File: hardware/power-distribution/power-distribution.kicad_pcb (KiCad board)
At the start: 2 copper layers, 100 x 100 mm, 54 parts, among them J1 Conn_01x02_Male, J10 Screw_Terminal_01x02, J11 Screw_Terminal_01x02, J12 Screw_Terminal_01x02, J13 Screw_Terminal_01x02, J14 Conn_01x02, J15 Screw_Terminal_01x06, J2 Conn_01x02_Male, J3 Conn_01x02_Male, J4 Conn_01x02_Male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

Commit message: Routed PCB
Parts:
- removed C1, C2, C3, C4, C5, C6: C, Capacitor_SMD:C_0603_1608Metric_Pad1.05x0.95mm_HandSolder
- removed F5, F6: Fuse, Highside-powerdistribution:ATO_Fuseholder_3522-2
- removed J10, J11, J12, J13, J8, J9: Screw_Terminal_01x02, Highside-powerdistribution:PTSA1,5-2-3,5-Z
- removed J14: Conn_01x02, Highside-powerdistribution:Phoenix_TB_2-1935776
- removed J15: Screw_Terminal_01x06, Highside-powerdistribution:20.101M-6
- removed J4, J5: Conn_01x02_Male, Connector_PinHeader_2.54mm:PinHeader_1x02_P2.54mm_Vertical
- removed Q5, Q6: P-MOSFET, Highside-powerdistribution:PG-TO263-3-2
- removed R10, R11, R12, R5, R6, R7, R8, R9: R, Resistor_SMD:R_0603_1608Metric_Pad1.05x0.95mm_HandSolder
- removed the REF** at (57.0, 91.0)
- removed the REF** at (146.5, 81.0)
- removed the REF** at (140.5, 76.0)
- removed the REF** at (52.5, 86.0)
- removed the REF** at (146.5, 53.5)
- removed the REF** at (53.5, 53.5)
- removed the REF** at (146.5, 146.5)
- removed the REF** at (146.5, 101.0)
- removed the REF** at (146.5, 91.0)
- removed the REF** at (140.5, 96.0)
- removed the REF** at (140.5, 86.0)
- added POWER_IN1: Screw_Terminal_01x02, TerminalBlock_Phoenix:TerminalBlock_Phoenix_PT-1,5-2-5.0-H_1x02_P5.00mm_Horizontal, F.Cu at (65.0, 105.0)
- added POWER_OUT1: Screw_Terminal_01x04, TerminalBlock_Phoenix:TerminalBlock_Phoenix_PT-1,5-4-5.0-H_1x04_P5.00mm_Horizontal, F.Cu at (120.0, 115.0)
- added REF**: MountingHole_3.2mm_M3_Pad_Via, MountingHole:MountingHole_3.2mm_M3_Pad_Via, F.Cu at (135.0, 85.0)
- added REF**: MountingHole_3.2mm_M3_Pad_Via, MountingHole:MountingHole_3.2mm_M3_Pad_Via, F.Cu at (135.0, 145.0)
- added REF**: MountingHole_3.2mm_M3_Pad_Via, MountingHole:MountingHole_3.2mm_M3_Pad_Via, F.Cu at (55.0, 145.0)
- added REF**: MountingHole_3.2mm_M3_Pad_Via, MountingHole:MountingHole_3.2mm_M3_Pad_Via, F.Cu at (55.0, 85.0)
- added SWITCH_A1: Screw_Terminal_01x0, TerminalBlock_Phoenix:TerminalBlock_Phoenix_PT-1,5-2-5.0-H_1x02_P5.00mm_Horizontal, F.Cu at (100.0, 137.5)
- added SWITCH_B1: Screw_Terminal_01x02, TerminalBlock_Phoenix:TerminalBlock_Phoenix_PT-1,5-2-5.0-H_1x02_P5.00mm_Horizontal, F.Cu at (87.5, 137.5)
- added SWITCH_C1: Screw_Terminal_01x02, TerminalBlock_Phoenix:TerminalBlock_Phoenix_PT-1,5-2-5.0-H_1x02_P5.00mm_Horizontal, F.Cu at (75.0, 137.5)
- added SWITCH_C2: Screw_Terminal_01x02, TerminalBlock_Phoenix:TerminalBlock_Phoenix_PT-1,5-2-5.0-H_1x02_P5.00mm_Horizontal, F.Cu at (62.5, 137.5)
- F1, F2, F3, F4: footprint Highside-powerdistribution:ATO_Fuseholder_3522-2 -> Private Fuses:ATO_Fuseholder_3522-2
- J1, J2, J3: value Conn_01x02_Male -> Parallell
- Q1, Q2, Q3, Q4: value P-MOSFET -> Q_PMOS_GDS; footprint Highside-powerdistribution:PG-TO263-3-2 -> Package_TO_SOT_SMD:TO-252-2
- R1, R2, R3, R4: value R -> 10k
- moved R4 25.6 mm to (67.5, 130.0), turned to 270 degrees
- moved R2 15.1 mm to (87.5, 130.0), turned to 270 degrees
- moved F4 14.5 mm to (102.5, 92.5)
- moved R3 13.4 mm to (80.0, 130.0), turned to 270 degrees
- moved F3 12.8 mm to (102.5, 102.5)
- moved Q4 11.4 mm to (85.0, 92.5), turned to 0 degrees
- moved F2 11.4 mm to (102.5, 112.5)
- moved F1 10.4 mm to (102.5, 122.5)
- moved Q3 8.99 mm to (85.4, 102.5), turned to 0 degrees
- moved Q2 7.11 mm to (85.0, 112.5), turned to 0 degrees
- moved J3 6.96 mm to (72.5, 130.0), turned to 270 degrees
- moved Q1 5.08 mm to (85.4, 122.5), turned to 0 degrees
- moved J2 4.30 mm to (85.0, 130.0), turned to 270 degrees
- moved R1 3.62 mm to (100.0, 130.0), turned to 270 degrees
- moved J1 2.55 mm to (97.5, 130.0), turned to 270 degrees
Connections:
- J1 pad 1: Net-(C1-Pad1) -> /G1
- J1 pad 2: Net-(C2-Pad1) -> Net-(J1-Pad2)
- J2 pad 1: Net-(C2-Pad1) -> Net-(J1-Pad2)
- J2 pad 2: Net-(C3-Pad1) -> Net-(J2-Pad2)
- J3 pad 1: Net-(C3-Pad1) -> Net-(J2-Pad2)
- J3 pad 2: Net-(C4-Pad1) -> Net-(J3-Pad2)
- Q1 pad 1: Net-(C1-Pad1) -> /G1
- Q1 pad 2: +12V -> SSR-A
- Q1 pad 3: SSR-A -> +12V
- Q2 pad 1: Net-(C2-Pad1) -> Net-(J1-Pad2)
- Q2 pad 2: +12V -> SSR-B
- Q2 pad 3: SSR-B -> +12V
- Q3 pad 1: Net-(C3-Pad1) -> Net-(J2-Pad2)
- Q3 pad 2: +12V -> SSR-C
- Q3 pad 3: SSR-C -> +12V
- Q4 pad 1: Net-(C4-Pad1) -> Net-(J3-Pad2)
- Q4 pad 2: +12V -> SSR-D
- Q4 pad 3: SSR-D -> +12V
- R1 pad 1: Net-(C1-Pad1) -> +12V
- R1 pad 2: +12V -> /G1
- R2 pad 1: Net-(J8-Pad1) -> +12V
- R2 pad 2: Net-(C1-Pad1) -> Net-(J1-Pad2)
- R3 pad 1: Net-(C2-Pad1) -> +12V
- R3 pad 2: +12V -> Net-(J2-Pad2)
- R4 pad 1: Net-(J9-Pad1) -> +12V
- R4 pad 2: Net-(C2-Pad1) -> Net-(J3-Pad2)
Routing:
- net Net-(C6-Pad1): track 103.5 -> 0.00 mm, vias 2 -> 0
- net GND: track 212.2 -> 111.8 mm, vias 6 -> 0
- net Net-(C5-Pad1): track 87.1 -> 0.00 mm, vias 2 -> 0
- net Net-(C4-Pad1): track 66.9 -> 0.00 mm, vias 2 -> 0
- net Net-(J3-Pad2): track 0.00 -> 60.4 mm, vias 0 -> 1
- net Net-(C3-Pad1): track 58.4 -> 0.00 mm, vias 2 -> 0
- net Net-(F1-Pad1): track 57.6 -> 0.00 mm
- net Net-(F6-Pad1): track 55.6 -> 0.00 mm
- net Net-(C2-Pad1): track 53.2 -> 0.00 mm, vias 2 -> 0
- net Net-(J2-Pad2): track 0.00 -> 49.3 mm, vias 0 -> 1
- net Net-(F5-Pad1): track 44.9 -> 0.00 mm
- net Net-(F2-Pad1): track 44.8 -> 0.00 mm
- net Net-(C1-Pad1): track 43.1 -> 0.00 mm, vias 2 -> 0
- net Net-(J1-Pad2): track 0.00 -> 39.5 mm, vias 0 -> 1
- net Net-(F3-Pad1): track 36.3 -> 0.00 mm
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- added copper zone on B.Cu, net Net-(F1-Pad1)
- added copper zone on F.Cu, net Net-(F1-Pad1)
- added copper zone on B.Cu, net Net-(F2-Pad1)
- added copper zone on F.Cu, net Net-(F2-Pad1)
- removed copper zone on B.Cu, net SSR-E
- removed copper zone on F.Cu, net SSR-E
- removed copper zone on B.Cu, net SSR-F
- removed copper zone on F.Cu, net SSR-F
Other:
- board size 100 x 100 mm -> 90 x 70 mm
- board text added: "MAX 18 A continuous (200 W)"
- board text added: "Rev 2 2020-03-12"
- board text removed: "E"
- board text removed: "F"
- board text removed: "Rev 1.3 2020-01-08"

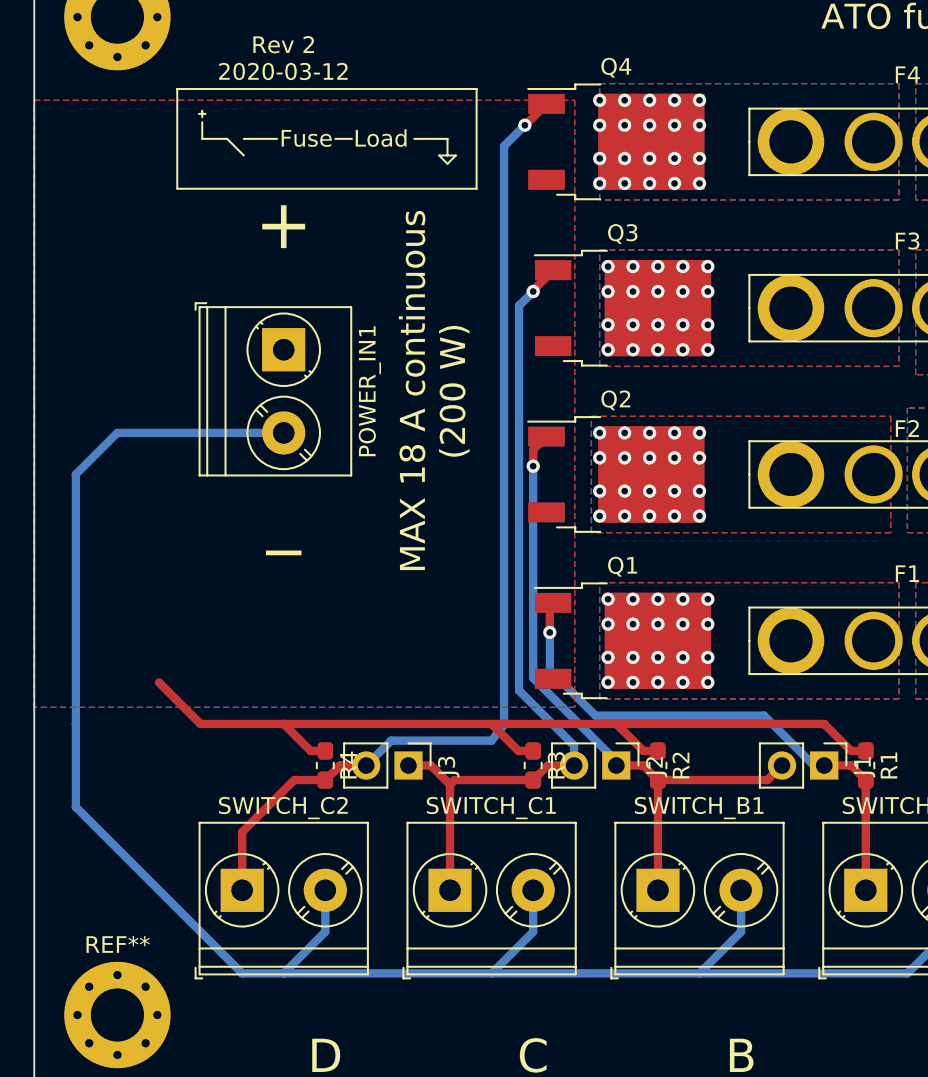
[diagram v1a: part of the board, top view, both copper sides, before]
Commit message: Runned ERC/DRC and exported gerber files
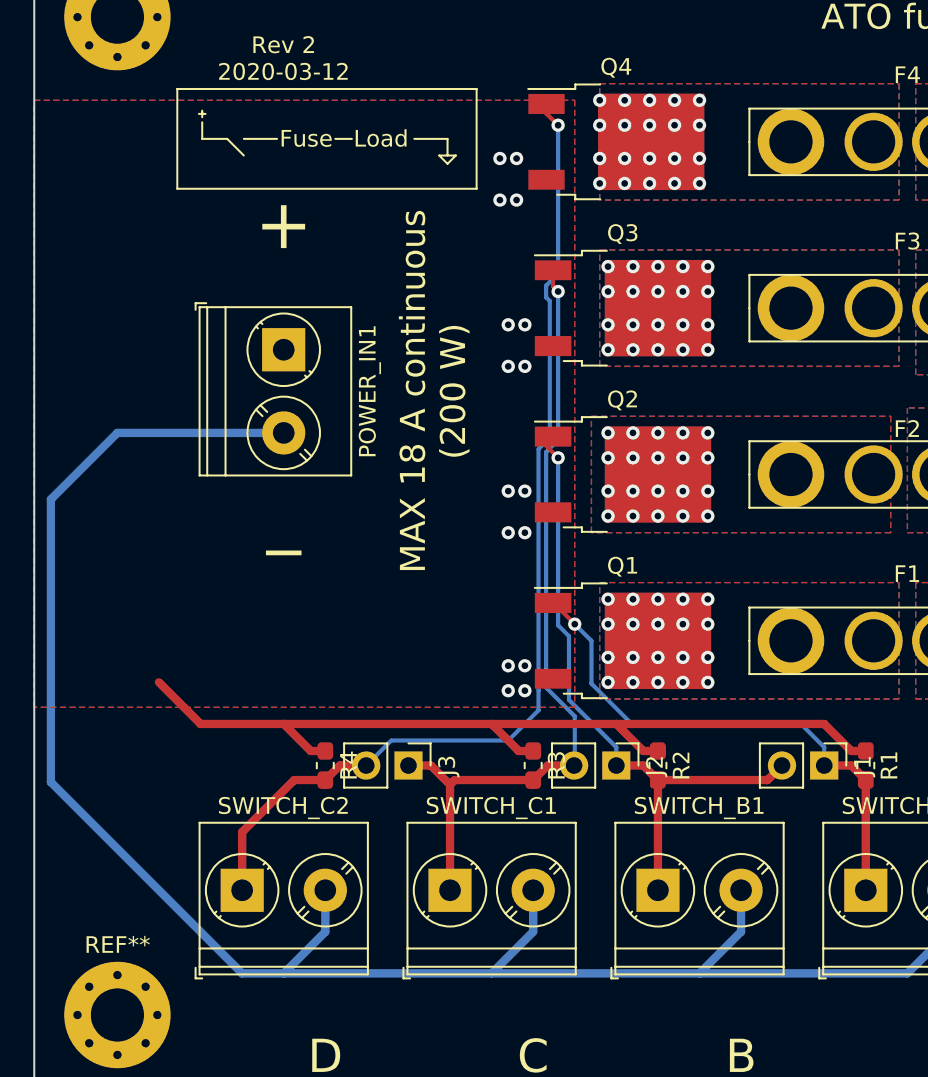
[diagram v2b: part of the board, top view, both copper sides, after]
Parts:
- moved Q2 0.40 mm to (85.4, 112.5)
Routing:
- net Net-(J3-Pad2): track 60.4 -> 61.7 mm
- net GND: track 111.8 -> 113.1 mm
- net Net-(J2-Pad2): track 49.3 -> 48.2 mm
- net Net-(J1-Pad2): track 39.5 -> 38.8 mm
- net +12V: vias 0 -> 16
